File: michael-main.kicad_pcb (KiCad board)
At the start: 4 copper layers, 98 x 119.8 mm, 183 parts, among them J1 Conn_01x03_Pin, J14 Conn_01x02_Pin, J15 Conn_01x02_Pin, J17 Conn_01x03_Pin, J18 Conn_01x05_Pin, J19 Conn_01x03_Pin, J21 Conn_01x05_Pin, J22 Conn_01x02_Pin, J25 Conn_01x09_Socket, J27 Conn_01x07_Socket, J28 XT30PW_2_2_-M.G.B, J29 XT30PW_2_2_-M.G.B, J3 Conn_01x03_Pin, J30 XT30PW_2_2_-M.G.B, J31 XT30PW_2_2_-M.G.B, J4 Conn_01x05_Pin, J5 Conn_01x05_Pin, J7 Conn_01x03_Pin, J8 USB_B_Mini, J9 Conn_01x05_Pin, Q1 BSC340N08NS3G, Q2 BSC340N08NS3G, Q3 BSC340N08NS3G, Q4 BSC340N08NS3G, U1 STM32F446RETx, U11 LMR14050SDDAR, U12 LMR14050SDDAR, U13 STM32F446RETx, U14 LM1084-5.0, U16 LM1084-3.3, U17 SN65HVD230, U18 SN65HVD230, U2 SN65HVD230, U3 STM32F446RETx, U4 SN65HVD230, U5 USBLC6-4SC6, U6 STM32F446RETx, U8 LTC7000EMSE-1_TRPBF, U9 STM32F446RETx, Y1 8Mhz, Y2 8Mhz, Y3 8Mhz, Y4 8Mhz, Y5 8Mhz

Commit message: competed
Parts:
- removed J15: Conn_01x02_Pin, Connector_PinHeader_2.54mm:PinHeader_1x02_P2.54mm_Vertical
- added C74: 0.1u, Capacitor_SMD:C_0805_2012Metric, F.Cu at (99.5, 148.2)
- added D10: 5.0SMDJ33A, Diode_SMD:D_SMC, F.Cu at (90.1, 163.9)
- added D5: LED, LED_SMD:LED_0603_1608Metric, F.Cu at (58.9, 82.3)
- added J6: Conn_01x03_Pin, Connector_JST:JST_XH_B3B-XH-A_1x03_P2.50mm_Vertical, F.Cu at (76.9, 144.7)
- added R37: 22, Resistor_SMD:R_0603_1608Metric, F.Cu at (79.1, 73.4)
- added R38: 22, Resistor_SMD:R_0603_1608Metric, F.Cu at (79.1, 70.7)
- added R39: 0, Resistor_SMD:R_0402_1005Metric, F.Cu at (92.0, 147.8)
- added R40: 0, Resistor_SMD:R_0402_1005Metric, F.Cu at (93.1, 147.8)
- added R41: 1k, Resistor_SMD:R_0603_1608Metric, F.Cu at (58.9, 79.1)
- C42, C51: footprint Capacitor_SMD:C_0805_2012Metric -> Capacitor_SMD:C_0603_1608Metric
- J14: footprint Connector_AMASS:AMASS_XT90PW-M_1x02_P10.90mm_Horizontal -> Connector_AMASS:AMASS_XT60PW-M_1x02_P7.20mm_Horizontal
- R12: footprint Resistor_SMD:R_2512_6332Metric -> wslp:RES_WSLP3921_.001OHM_VIS-L
- R16: footprint Resistor_SMD:R_0805_2012Metric -> Resistor_SMD:R_0603_1608Metric
- R17: value 0 -> 33k
- R18: value 0 -> 22
- moved R22 37.2 mm to (124.3, 70.0)
- moved C70 33.9 mm to (124.2, 75.2)
- moved C65 31.2 mm to (92.4, 135.2), turned to 90 degrees
- moved J25 30.0 mm to (84.0, 71.5)
- moved J27 30.0 mm to (101.8, 71.5)
- moved C78 28.4 mm to (97.9, 135.2), turned to 90 degrees
- moved R1 27.1 mm to (124.3, 68.7)
- moved R34 27.1 mm to (104.0, 104.9), turned to 0 degrees
- moved C29 26.8 mm to (85.0, 81.2)
- moved C31 26.8 mm to (85.0, 84.5)
- moved Y1 26.8 mm to (81.2, 80.4)
- moved R27 26.6 mm to (104.0, 119.5), turned to 0 degrees
- moved J17 26.6 mm to (106.4, 62.1), turned to 90 degrees
- moved C6 26.2 mm to (104.0, 118.3)
- moved C10 26.2 mm to (104.0, 117.2)
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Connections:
- R11 pad 1: Net-(J15-Pin_1) -> /PWR_CTL_IN
- U3 pad 21: /SPI_SCK -> Net-(U3-PA5)
- U3 pad 23: /SPI_MOSI -> Net-(U3-PA7)
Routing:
- net GND: track 327.8 -> 490.1 mm, vias 36 -> 176
- net +BATT: track 0.00 -> 88.3 mm, vias 0 -> 1
- net /CS3: track 1.90 -> 87.0 mm, vias 0 -> 2
- net /SPI_MISO: track 0.00 -> 83.6 mm, vias 0 -> 5
- net /SPI_MOSI: track 0.00 -> 81.9 mm, vias 0 -> 5
- net /SPI_SCK: track 0.00 -> 78.6 mm, vias 0 -> 5
- net /CS2: track 2.07 -> 79.9 mm, vias 0 -> 2
- net Net-(C74-Pad2): track 0.00 -> 67.5 mm, vias 0 -> 9
- net /CS1: track 1.80 -> 65.8 mm, vias 0 -> 2
- net +3.3V: track 169.2 -> 229.6 mm, vias 61 -> 62
- net Net-(U13-BOOT0): track 14.0 -> 72.1 mm
- net GNDPWR: track 38.4 -> 94.2 mm, vias 50 -> 41
- net /CS0: track 2.00 -> 51.3 mm, vias 0 -> 2
- net Net-(U1-BOOT0): track 12.6 -> 59.7 mm
- net /sen-: track 0.00 -> 47.1 mm
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- added copper zone on F.Cu, net GND
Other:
- board size 98 x 119.8 mm -> 99 x 113 mm
- board text added: "BUS0"
- board text added: "BUS1"
- board text added: "BUS2"
- board text added: "BUS3"

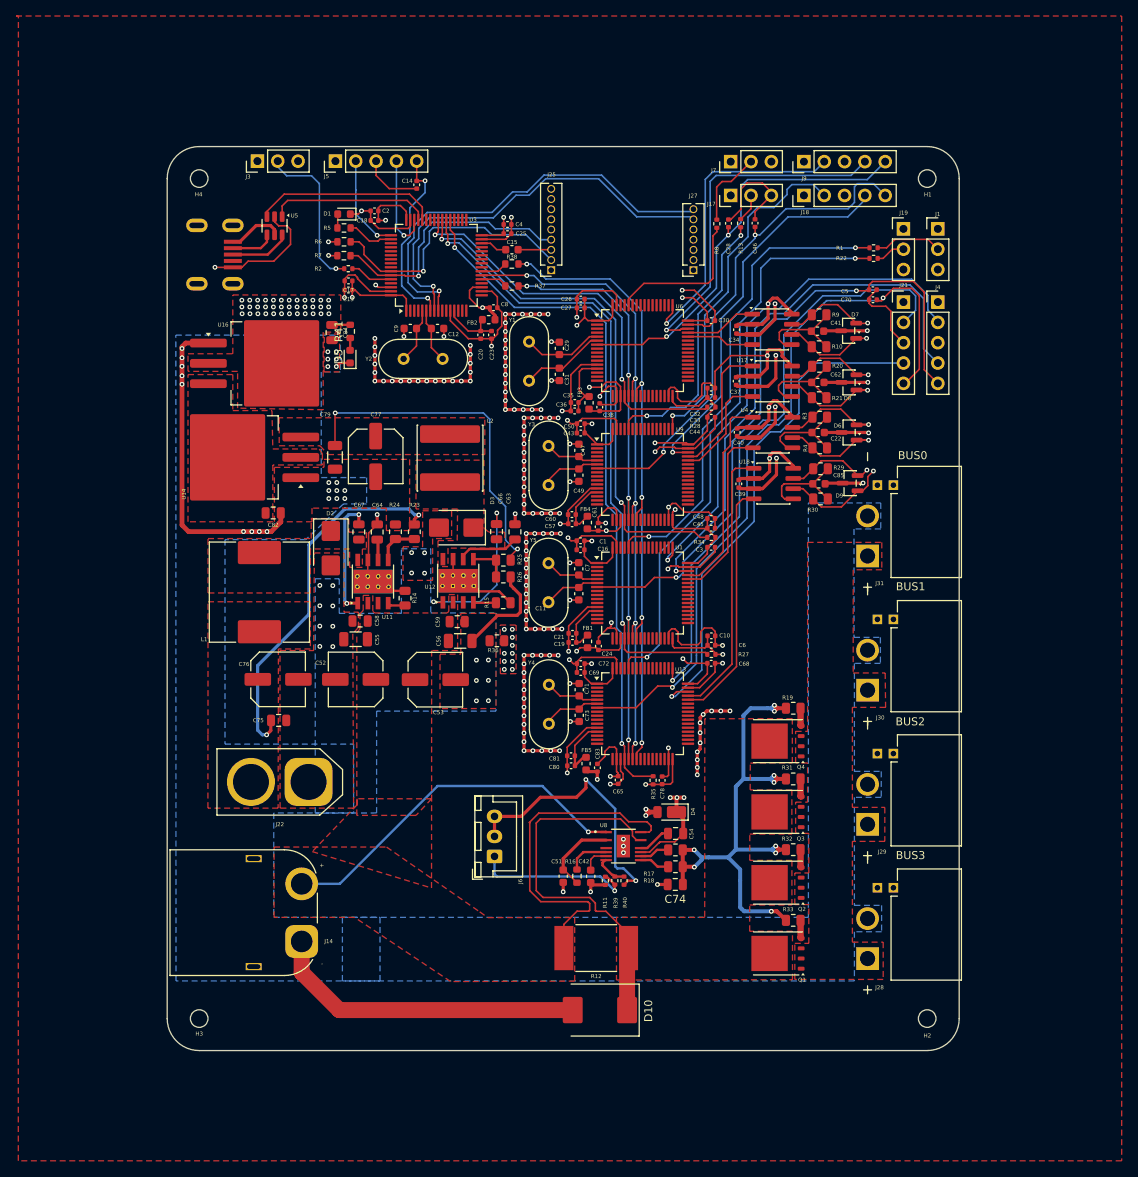
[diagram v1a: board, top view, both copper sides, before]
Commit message: updated vcap, reworked on power plane, added debug led and uart to 1 slave
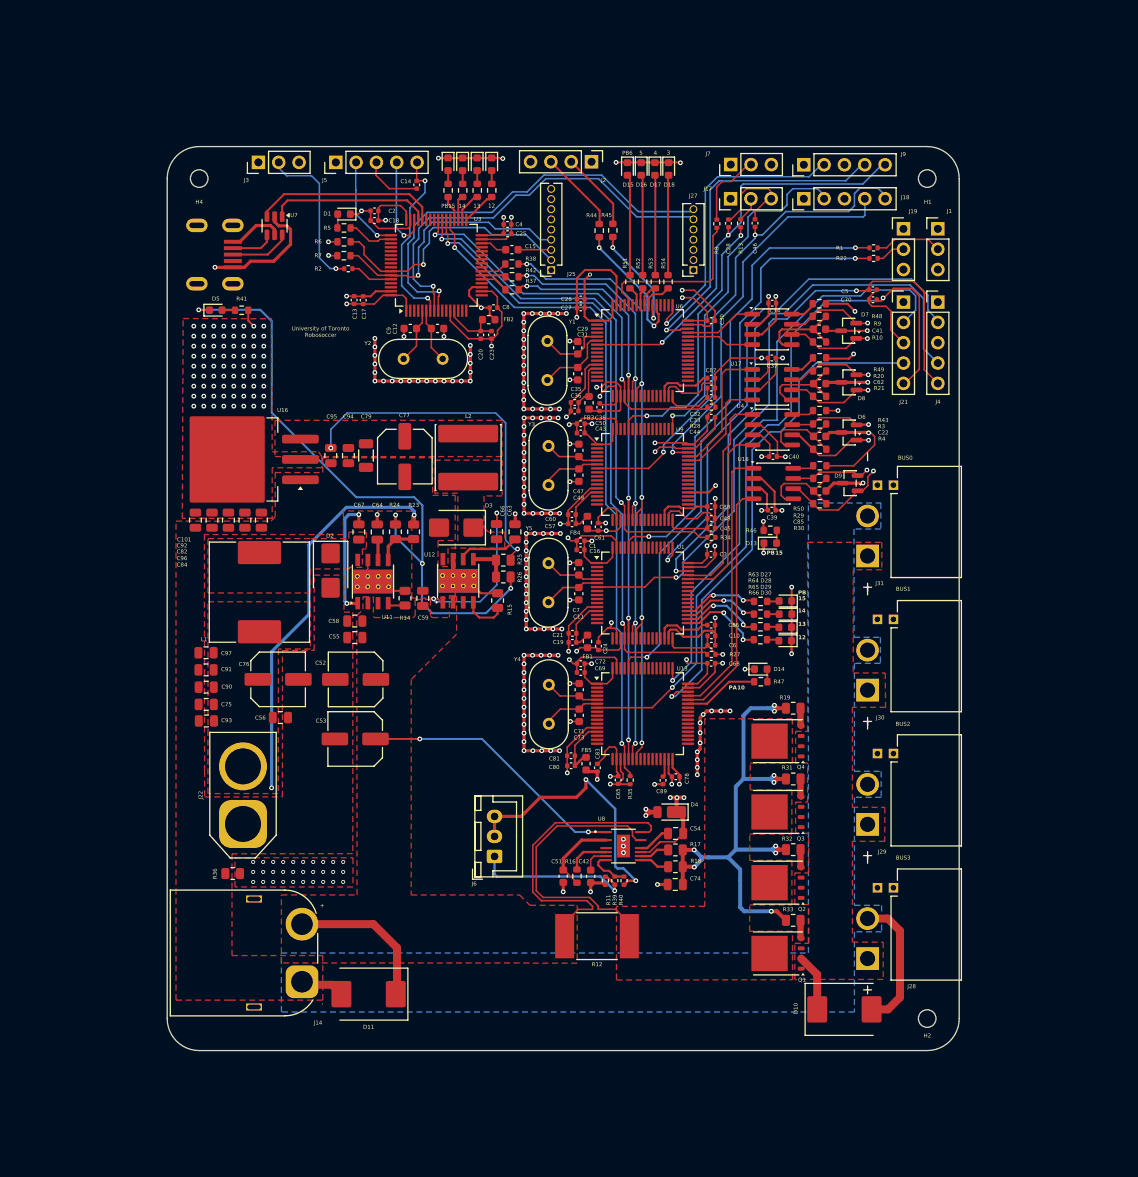
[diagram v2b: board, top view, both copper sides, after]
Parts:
- removed H3: MountingHole, MountingHole:MountingHole_2.2mm_M2
- removed U14: LM1084-5.0, Package_TO_SOT_SMD:TO-263-3_TabPin2
- removed U5: USBLC6-4SC6, Package_TO_SOT_SMD:SOT-23-6
- added C101: 0.1u, Capacitor_SMD:C_0805_2012Metric, F.Cu at (39.5, 102.7)
- added C86: 4.7uF, Capacitor_SMD:C_0402_1005Metric, F.Cu at (104.0, 115.8)
- added C87: 4.7uF, Capacitor_SMD:C_0402_1005Metric, F.Cu at (104.0, 85.0)
- added C88: 4.7uF, Capacitor_SMD:C_0402_1005Metric, F.Cu at (104.0, 101.0)
- added C89: 4.7uF, Capacitor_SMD:C_0402_1005Metric, F.Cu at (98.0, 135.2)
- added C90: 0.1u, Capacitor_SMD:C_0805_2012Metric, F.Cu at (40.9, 123.6)
- added C91: 0.1u, Capacitor_SMD:C_0805_2012Metric, F.Cu at (40.9, 121.4)
- added C92: 0.1u, Capacitor_SMD:C_0805_2012Metric, F.Cu at (41.6, 102.7)
- added C93: 1n, Capacitor_SMD:C_0805_2012Metric, F.Cu at (40.9, 127.8)
- added C94: 0.1u, Capacitor_SMD:C_0805_2012Metric, F.Cu at (58.6, 94.6)
- added C95: 0.1u, Capacitor_SMD:C_0805_2012Metric, F.Cu at (56.5, 94.6)
- added C96: 10uF, Capacitor_SMD:C_0805_2012Metric, F.Cu at (45.7, 102.7)
- added C97: 10u, Capacitor_SMD:C_0805_2012Metric, F.Cu at (40.9, 119.3)
- added D11: 5.0SMDJ33A, Diode_SMD:D_SMC, F.Cu at (61.2, 161.9)
- added D13: LED, LED_SMD:LED_0603_1608Metric, F.Cu at (111.4, 105.6)
- added D14: LED, LED_SMD:LED_0603_1608Metric, F.Cu at (110.2, 121.3)
- added D15: LED, LED_SMD:LED_0603_1608Metric, F.Cu at (93.5, 58.8)
- added D16: LED, LED_SMD:LED_0603_1608Metric, F.Cu at (95.2, 58.8)
- added D17: LED, LED_SMD:LED_0603_1608Metric, F.Cu at (97.0, 58.8)
- added D18: LED, LED_SMD:LED_0603_1608Metric, F.Cu at (98.7, 58.8)
- added D19: LED, LED_SMD:LED_0603_1608Metric, F.Cu at (71.1, 58.2)
- added D20: LED, LED_SMD:LED_0603_1608Metric, F.Cu at (72.9, 58.2)
- added D21: LED, LED_SMD:LED_0603_1608Metric, F.Cu at (74.7, 58.2)
- added D22: LED, LED_SMD:LED_0603_1608Metric, F.Cu at (76.6, 58.2)
- added D27: LED, LED_SMD:LED_0603_1608Metric, F.Cu at (113.3, 112.8)
- added D28: LED, LED_SMD:LED_0603_1608Metric, F.Cu at (113.3, 114.5)
- added D29: LED, LED_SMD:LED_0603_1608Metric, F.Cu at (113.2, 116.1)
- added D30: LED, LED_SMD:LED_0603_1608Metric, F.Cu at (113.2, 117.8)
- added J2: Conn_01x04_Pin, Connector_PinHeader_2.54mm:PinHeader_1x04_P2.54mm_Vertical, F.Cu at (89.0, 57.9)
- added R42: 22, Resistor_SMD:R_0603_1608Metric, F.Cu at (79.1, 72.3)
- added R43: 0, Resistor_SMD:R_0603_1608Metric, F.Cu at (117.5, 89.0)
- added R44: 11, Resistor_SMD:R_0603_1608Metric, F.Cu at (90.0, 66.5)
- added R45: 11, Resistor_SMD:R_0603_1608Metric, F.Cu at (91.7, 66.5)
- added R46: 1k, Resistor_SMD:R_0603_1608Metric, F.Cu at (111.4, 104.0)
- added R47: 1k, Resistor_SMD:R_0603_1608Metric, F.Cu at (110.2, 122.9)
- added R48: 0, Resistor_SMD:R_0603_1608Metric, F.Cu at (117.5, 75.7)
- added R49: 0, Resistor_SMD:R_0603_1608Metric, F.Cu at (117.5, 82.4)
- added R50: 0, Resistor_SMD:R_0603_1608Metric, F.Cu at (117.6, 95.9)
- added R51: 1k, Resistor_SMD:R_0603_1608Metric, F.Cu at (93.8, 72.9)
- added R52: 1k, Resistor_SMD:R_0603_1608Metric, F.Cu at (95.4, 72.9)
- added R53: 1k, Resistor_SMD:R_0603_1608Metric, F.Cu at (97.0, 72.9)
- added R54: 1k, Resistor_SMD:R_0603_1608Metric, F.Cu at (98.6, 72.9)
- added R55: 1k, Resistor_SMD:R_0603_1608Metric, F.Cu at (71.1, 61.5)
- added R56: 1k, Resistor_SMD:R_0603_1608Metric, F.Cu at (72.9, 61.5)
- added R57: 1k, Resistor_SMD:R_0603_1608Metric, F.Cu at (74.8, 61.5)
- added R58: 1k, Resistor_SMD:R_0603_1608Metric, F.Cu at (76.6, 61.5)
- added R63: 1k, Resistor_SMD:R_0603_1608Metric, F.Cu at (110.2, 112.9)
- added R64: 1k, Resistor_SMD:R_0603_1608Metric, F.Cu at (110.2, 114.4)
- added R65: 1k, Resistor_SMD:R_0603_1608Metric, F.Cu at (110.2, 116.0)
- added R66: 1k, Resistor_SMD:R_0603_1608Metric, F.Cu at (110.2, 117.6)
- added U7: USBLC6-2SC6, Package_TO_SOT_SMD:SOT-23-6, F.Cu at (49.4, 65.9)
- C10, C13, C14, C16, C17, C18, C21, C23, C27, C28, C3, C30, C32, C33, C34, C36, C37, C39, C4, C40, C44, C45, C46, C48, C5, C50, C6, C60, C68, C69, C70, C72, C78, C8, C81: value 0.1uF -> 0.1u
- C55: footprint Capacitor_SMD:C_1206_3216Metric -> Capacitor_SMD:C_0805_2012Metric
- C56: value 10u -> 1n; footprint Capacitor_SMD:C_1206_3216Metric -> Capacitor_SMD:C_0805_2012Metric
- C82: value 10uF -> 0.1u
- R10, R20, R21, R29, R3, R30, R4, R9: value 60 -> 75; footprint Resistor_SMD:R_0805_2012Metric -> Resistor_SMD:R_0603_1608Metric
- R41: value 1k -> 8k
- moved R36 44.0 mm to (44.2, 146.9)
- moved D10 30.6 mm to (120.7, 163.8), turned to 0 degrees
- moved C84 25.1 mm to (47.8, 102.7)
- moved C56 24.4 mm to (50.1, 127.4)
- moved D5 17.8 mm to (42.1, 76.5), turned to 0 degrees
- moved R41 13.8 mm to (45.3, 76.5), turned to 0 degrees
- moved U16 12.6 mm to (45.0, 95.1), turned to 180 degrees
- moved C53 12.5 mm to (59.5, 130.1), turned to 180 degrees
- moved J22 9.74 mm to (45.5, 140.7), turned to 90 degrees
- moved C75 9.27 mm to (40.9, 125.7), turned to 180 degrees
- moved C82 5.67 mm to (43.6, 102.7), turned to -90 degrees
- moved C34 5.56 mm to (111.6, 75.6), turned to 180 degrees
- moved C40 5.41 mm to (111.7, 94.8), turned to 0 degrees
- moved C37 5.31 mm to (111.6, 82.4), turned to 180 degrees
- moved C39 5.28 mm to (111.6, 101.5), turned to 0 degrees
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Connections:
- C56 pad 1: +BATT -> +15V
- C82 pad 1: +5V -> +3.3V
- D10 pad 1: /sen- -> +24V
- U1 pad 30: unconnected-(U1-VCAP_1-Pad30) -> Net-(U1-VCAP_1)
- U1 pad 33: unconnected-(U1-PB12-Pad33) -> Net-(U1-PB12)
- U1 pad 34: unconnected-(U1-PB13-Pad34) -> Net-(U1-PB13)
- U1 pad 35: unconnected-(U1-PB14-Pad35) -> Net-(U1-PB14)
- U1 pad 36: unconnected-(U1-PB15-Pad36) -> Net-(U1-PB15)
- U13 pad 30: unconnected-(U13-VCAP_1-Pad30) -> Net-(U13-VCAP_1)
- U13 pad 43: unconnected-(U13-PA10-Pad43) -> Net-(U13-PA10)
- U16 pad 3: +5V -> +6V
- U17 pad 8: GND -> Net-(U17-Rs)
- U18 pad 8: GND -> Net-(U18-Rs)
- U2 pad 8: GND -> Net-(U2-Rs)
- U3 pad 22: /SPI_MISO -> Net-(U3-PA6)
- U3 pad 33: unconnected-(U3-PB12-Pad33) -> Net-(U3-PB12)
- U3 pad 34: unconnected-(U3-PB13-Pad34) -> Net-(U3-PB13)
- U3 pad 35: unconnected-(U3-PB14-Pad35) -> Net-(U3-PB14)
- U3 pad 36: unconnected-(U3-PB15-Pad36) -> Net-(U3-PB15)
- U4 pad 8: GND -> Net-(U4-Rs)
- U6 pad 30: unconnected-(U6-VCAP_1-Pad30) -> Net-(U6-VCAP_1)
- U6 pad 53: unconnected-(U6-PC12-Pad53) -> /Slave_tx
- U6 pad 54: unconnected-(U6-PD2-Pad54) -> /Slave_rx
- U6 pad 55: unconnected-(U6-PB3-Pad55) -> Net-(U6-PB3)
- U6 pad 56: unconnected-(U6-PB4-Pad56) -> Net-(U6-PB4)
- U6 pad 57: unconnected-(U6-PB5-Pad57) -> Net-(U6-PB5)
- U6 pad 58: unconnected-(U6-PB6-Pad58) -> Net-(U6-PB6)
- U9 pad 30: unconnected-(U9-VCAP_1-Pad30) -> Net-(U9-VCAP_1)
- U9 pad 36: unconnected-(U9-PB15-Pad36) -> Net-(U9-PB15)
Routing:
- net /Slave_tx: track 0.00 -> 16.9 mm, vias 0 -> 2
- net /Slave_rx: track 0.00 -> 14.0 mm, vias 0 -> 2
- net GND: track 490.1 -> 504.0 mm, vias 176 -> 208
- net Net-(U9-PB15): track 0.00 -> 12.8 mm, vias 0 -> 2
- net Net-(D15-A): track 0.00 -> 12.6 mm
- net Net-(D16-A): track 0.00 -> 12.6 mm
- net Net-(D18-A): track 0.00 -> 12.5 mm
- net Net-(D17-A): track 0.00 -> 12.5 mm
- net +3.3V: track 229.6 -> 217.9 mm, vias 62 -> 98
- net /sen-: track 47.1 -> 35.9 mm
- net Net-(U1-PB12): track 0.00 -> 10.8 mm, vias 0 -> 2
- net Net-(J2-Pin_3): track 0.00 -> 10.3 mm
- net Net-(U1-PB13): track 0.00 -> 10.2 mm, vias 0 -> 2
- net GNDPWR: track 94.2 -> 104.1 mm, vias 41 -> 4
- net Net-(J2-Pin_2): track 0.00 -> 9.95 mm
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- removed copper zone on F.Cu, net +5V
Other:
- board text added: "10"
- board text added: "12"
- board text added: "13"
- board text added: "14"
- board text added: "15"
- board text added: "3"
- board text added: "4"
- board text added: "5"
- board text added: "PA"
- board text added: "PB"
- board text added: "PB15"
- board text added: "PB6"
- board text added: "University of Toronto Robosoccer"
